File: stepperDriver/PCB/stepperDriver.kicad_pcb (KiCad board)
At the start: 2 copper layers, 33.9 x 20 mm, 11 parts, among them J1 grove, M1 Stepper_Motor_bipolar, U1 EL814, U2 ATtiny45-20PU

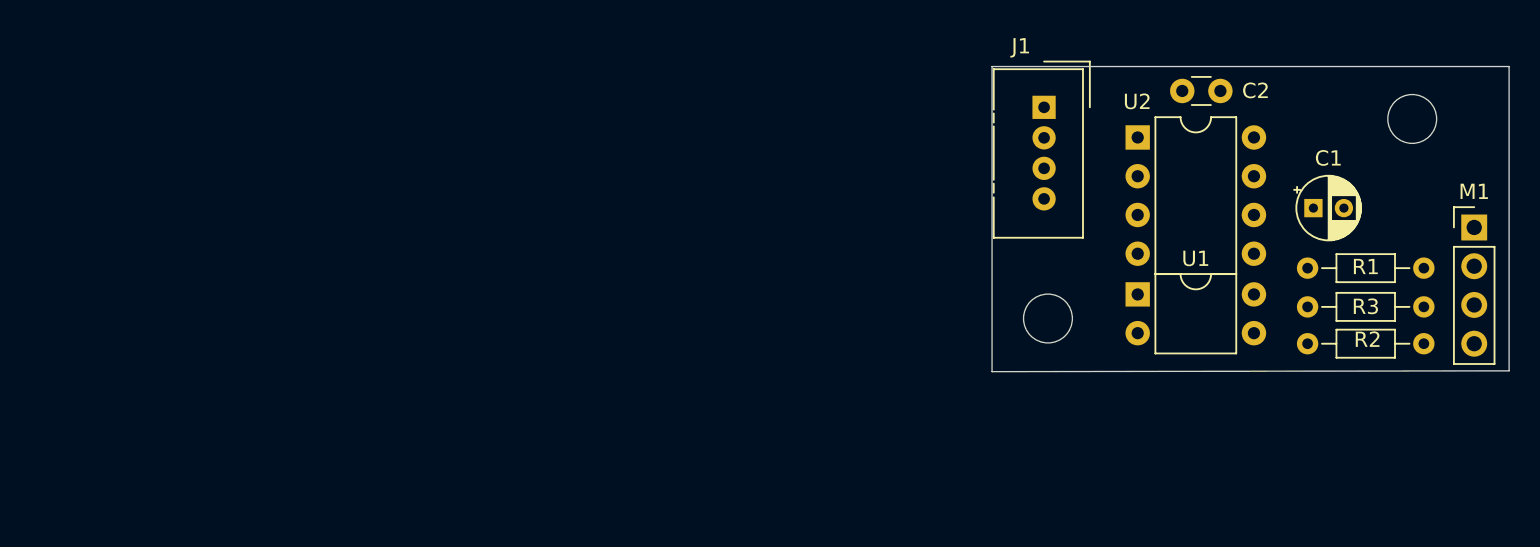
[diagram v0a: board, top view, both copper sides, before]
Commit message: changed schematic and made new PCB. I removed the DCC interface and rectifier
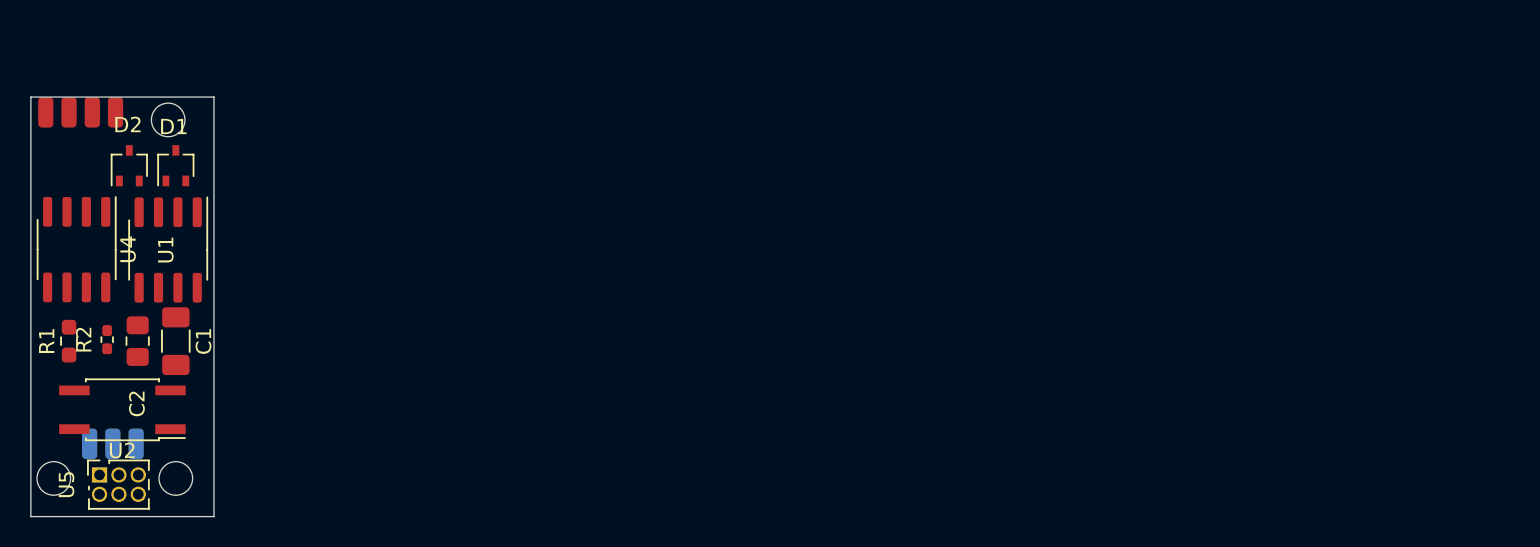
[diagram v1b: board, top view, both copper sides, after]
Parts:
- removed M1: Stepper_Motor_bipolar, Connector_PinHeader_2.54mm:PinHeader_1x04_P2.54mm_Vertical
- removed R3: R, Resistor_THT:R_Axial_DIN0204_L3.6mm_D1.6mm_P7.62mm_Horizontal
- removed the REF** at (201.0, 122.9)
- removed the REF** at (177.2, 136.0)
- added D1: BAT54CW, Package_TO_SOT_SMD:SOT-323_SC-70, F.Cu at (120.0, 126.0)
- added D2: BAT54CW, Package_TO_SOT_SMD:SOT-323_SC-70, F.Cu at (117.0, 126.0)
- added J2: pin, Connector_Wire:SolderWirePad_1x01_SMD_1x2mm, B.Cu at (115.9, 144.2)
- added J3: pin, Connector_Wire:SolderWirePad_1x01_SMD_1x2mm, B.Cu at (114.3, 144.2)
- added J4: mot, Connector_Wire:SolderWirePad_1x01_SMD_1x2mm, F.Cu at (116.0, 122.5)
- added J5: mot, Connector_Wire:SolderWirePad_1x01_SMD_1x2mm, F.Cu at (114.5, 122.5)
- added J6: mot, Connector_Wire:SolderWirePad_1x01_SMD_1x2mm, F.Cu at (113.0, 122.5)
- added J7: mot, Connector_Wire:SolderWirePad_1x01_SMD_1x2mm, F.Cu at (111.5, 122.5)
- added REF**: MountingHole_2.2mm_M2, MountingHole:MountingHole_2.2mm_M2, F.Cu at (112.0, 146.5)
- added REF**: MountingHole_2.2mm_M2, MountingHole:MountingHole_2.2mm_M2, F.Cu at (120.0, 146.5)
- added REF**: MountingHole_2.2mm_M2, MountingHole:MountingHole_2.2mm_M2, F.Cu at (119.5, 123.0)
- added U4: ATtiny13A-SS, Package_SO:SOIC-8_3.9x4.9mm_P1.27mm, F.Cu at (113.5, 131.5)
- added U5: HEADER_3x2, Connector_PinSocket_1.27mm:PinSocket_2x03_P1.27mm_Vertical, F.Cu at (115.0, 146.3)
- C1: footprint Capacitor_THT:CP_Radial_D4.0mm_P2.00mm -> Capacitor_SMD:C_1206_3216Metric_Pad1.33x1.80mm_HandSolder
- C2: footprint Capacitor_THT:C_Disc_D3.0mm_W1.6mm_P2.50mm -> Capacitor_SMD:C_0805_2012Metric_Pad1.18x1.45mm_HandSolder
- J1: value grove -> pin; footprint Connector:NS-Tech_Grove_1x04_P2mm_Vertical -> Connector_Wire:SolderWirePad_1x01_SMD_1x2mm; moved to B.Cu
- R1: value 1k -> 1k5; footprint Resistor_THT:R_Axial_DIN0204_L3.6mm_D1.6mm_P7.62mm_Horizontal -> Resistor_SMD:R_0603_1608Metric_Pad0.98x0.95mm_HandSolder
- R2: footprint Resistor_THT:R_Axial_DIN0204_L3.6mm_D1.6mm_P7.62mm_Horizontal -> Resistor_SMD:R_0402_1005Metric_Pad0.72x0.64mm_HandSolder
- U1: value EL814 -> L78L05_SO8; footprint Package_DIP:DIP-4_W7.62mm -> Package_SO:SOIC-8_3.9x4.9mm_P1.27mm
- U2: value ATtiny45-20PU -> LTV-357T; footprint Package_DIP:DIP-8_W7.62mm -> Package_SO:SO-4_4.4x3.6mm_P2.54mm
- moved R1 81.3 mm to (113.0, 137.5), turned to 90 degrees
- moved R2 78.7 mm to (115.5, 137.4), turned to -90 degrees
- moved C1 75.1 mm to (120.0, 137.5), turned to -90 degrees
- moved C2 72.8 mm to (117.5, 137.5), turned to -90 degrees
- moved U2 68.9 mm to (116.5, 142.0), turned to 180 degrees
- moved U1 63.6 mm to (119.5, 131.5), turned to -90 degrees
- moved J1 63.5 mm to (117.4, 144.2), turned to 180 degrees
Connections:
- C1 pad 1: +5V -> VCC
- J1 pad 1: Net-(J1-Pad1) -> VCC
- R1 pad 1: Net-(R1-Pad1) -> VCC
- R1 pad 2: Net-(J1-Pad1) -> Net-(R1-Pad2)
- R2 pad 1: Net-(R2-Pad1) -> +5V
- R2 pad 2: Net-(M1-Pad3) -> /RESET
- U1 pad 1: Net-(R1-Pad1) -> +5V
- U1 pad 2: Net-(J1-Pad2) -> GND
- U1 pad 4: /IN -> unconnected-(U1-Pad4)
- U2 pad 1: Net-(U2-Pad1) -> Net-(R1-Pad2)
- U2 pad 2: Net-(R2-Pad1) -> Net-(J2-Pad1)
- U2 pad 3: Net-(M1-Pad4) -> GND
- U2 pad 4: GND -> /IN
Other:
- board size 33.9 x 20 mm -> 12 x 27.5 mm
- net class Default removed
